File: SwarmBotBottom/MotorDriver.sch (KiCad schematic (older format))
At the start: 12 parts, among them U3 STSPIN220

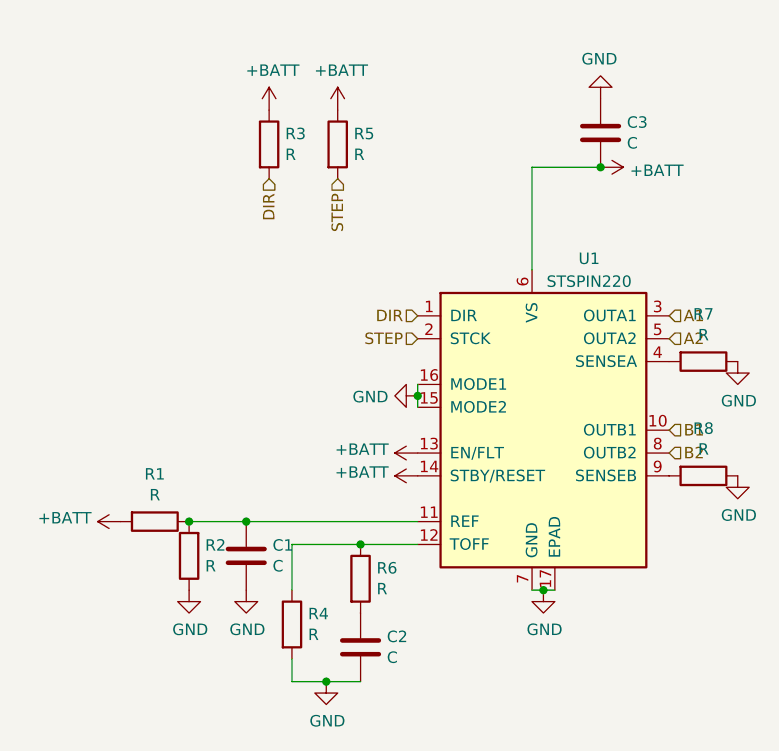
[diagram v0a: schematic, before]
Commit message: Camera routing with all sensors and motors
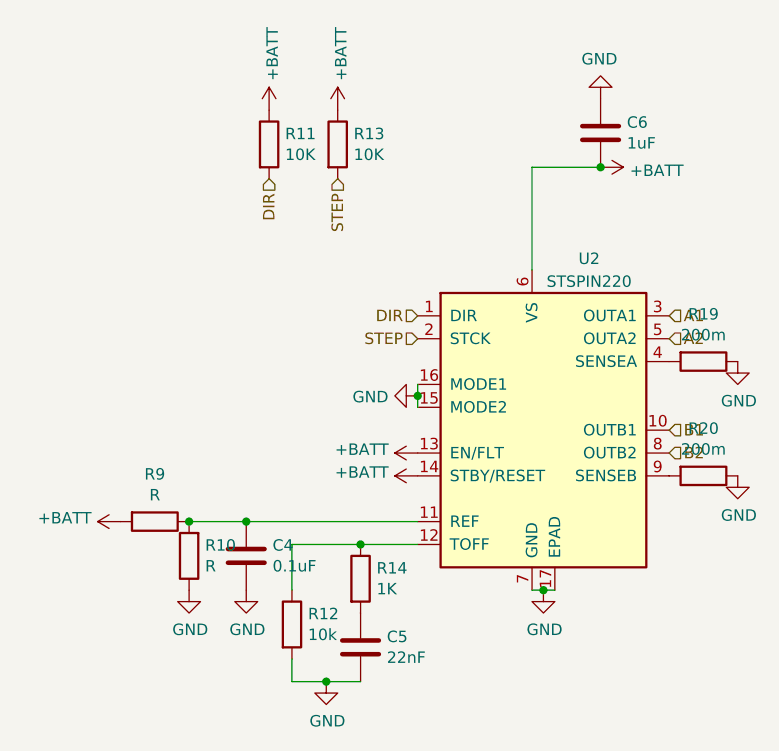
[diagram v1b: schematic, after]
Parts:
- C10: renamed from C1; value C -> 0.1uF
- C11: renamed from C2; value C -> 22nF
- C17: renamed from C3; value C -> 1uF
- R11: renamed from R3; value R -> 10K
- R12: renamed from R4; value R -> 10k
- R13: renamed from R5; value R -> 10K
- R14: renamed from R6; value R -> 1K
- R15: renamed from R7; value R -> 200m
- R16: renamed from R8; value R -> 200m
- U3: footprint Package_DFN_QFN:QFN-16-1EP_3x3mm_P0.5mm_EP1.8x1.8mm -> Package_DFN_QFN:VQFN-16-1EP_3x3mm_P0.5mm_EP1.8x1.8mm
- renumbered R1 to R8, R2 to R9

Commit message: things
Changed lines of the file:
@@
 $Descr A4 11693 8268
 encoding utf-8
-Sheet 4 4
+Sheet 3 4
 Title ""
 Date ""
@@
 AR Path="/5DAF9EF2/5DFB20FE/5DE73FE9" Ref="U1"  Part="1"
 AR Path="/5DAF9EF2/5DFB6676/5DE73FE9" Ref="U2"  Part="1"
-F 0 "U2" H 5050 3700 50  0000 C CNN
+F 0 "U1" H 5050 3700 50  0000 C CNN
 F 1 "STSPIN220" H 5050 3600 50  0000 C CNN
 F 2 "Package_DFN_QFN:VQFN-16-1EP_3x3mm_P0.5mm_EP1.8x1.8mm" H 5000 3700 50  0001 L CNN
@@
 AR Path="/5DAF9EF2/5DFB20FE/5DE7927A" Ref="R3"  Part="1"
 AR Path="/5DAF9EF2/5DFB6676/5DE7927A" Ref="R11"  Part="1"
-F 0 "R11" H 3720 1746 50  0000 L CNN
+F 0 "R3" H 3720 1746 50  0000 L CNN
 F 1 "10K" H 3720 1655 50  0000 L CNN
 F 2 "Resistor_SMD:R_0402_1005Metric" V 3580 1700 50  0001 C CNN
@@
 AR Path="/5DAF9EF2/5DFB20FE/5DE792A2" Ref="R5"  Part="1"
 AR Path="/5DAF9EF2/5DFB6676/5DE792A2" Ref="R13"  Part="1"
-F 0 "R13" H 4020 1746 50  0000 L CNN
+F 0 "R5" H 4020 1746 50  0000 L CNN
 F 1 "10K" H 4020 1655 50  0000 L CNN
 F 2 "Resistor_SMD:R_0402_1005Metric" V 3880 1700 50  0001 C CNN
@@
 AR Path="/5DAF9EF2/5DFB20FE/5DE796BD" Ref="#PWR0105"  Part="1"
 AR Path="/5DAF9EF2/5DFB6676/5DE796BD" Ref="#PWR0119"  Part="1"
-F 0 "#PWR0119" H 4300 2550 50  0001 C CNN
+F 0 "#PWR0105" H 4300 2550 50  0001 C CNN
 F 1 "GND" V 4305 2672 50  0000 R CNN
 F 2 "" H 4300 2800 50  0001 C CNN
@@
 AR Path="/5DAF9EF2/5DFB20FE/5DE79796" Ref="#PWR0106"  Part="1"
 AR Path="/5DAF9EF2/5DFB6676/5DE79796" Ref="#PWR0120"  Part="1"
-F 0 "#PWR0120" H 4300 2900 50  0001 C CNN
+F 0 "#PWR0106" H 4300 2900 50  0001 C CNN
 F 1 "+BATT" V 4315 3177 50  0000 L CNN
 F 2 "" H 4300 3050 50  0001 C CNN
@@
 AR Path="/5DAF9EF2/5DFB20FE/5DE797D2" Ref="#PWR0107"  Part="1"
 AR Path="/5DAF9EF2/5DFB6676/5DE797D2" Ref="#PWR0121"  Part="1"
-F 0 "#PWR0121" H 4300 3000 50  0001 C CNN
+F 0 "#PWR0107" H 4300 3000 50  0001 C CNN
 F 1 "+BATT" V 4315 3277 50  0000 L CNN
 F 2 "" H 4300 3150 50  0001 C CNN
@@
 AR Path="/5DAF9EF2/5DFB20FE/5DE7980C" Ref="R6"  Part="1"
 AR Path="/5DAF9EF2/5DFB6676/5DE7980C" Ref="R14"  Part="1"
-F 0 "R14" H 4120 3646 50  0000 L CNN
+F 0 "R6" H 4120 3646 50  0000 L CNN
 F 1 "1K" H 4120 3555 50  0000 L CNN
 F 2 "Resistor_SMD:R_0402_1005Metric" V 3980 3600 50  0001 C CNN
@@
 AR Path="/5DAF9EF2/5DFB20FE/5DE79862" Ref="C2"  Part="1"
 AR Path="/5DAF9EF2/5DFB6676/5DE79862" Ref="C5"  Part="1"
-F 0 "C5" H 4165 3946 50  0000 L CNN
+F 0 "C2" H 4165 3946 50  0000 L CNN
 F 1 "22nF" H 4165 3855 50  0000 L CNN
 F 2 "Capacitor_SMD:C_0402_1005Metric" H 4088 3750 50  0001 C CNN
@@
 AR Path="/5DAF9EF2/5DFB20FE/5DE798BA" Ref="R4"  Part="1"
 AR Path="/5DAF9EF2/5DFB6676/5DE798BA" Ref="R12"  Part="1"
-F 0 "R12" H 3820 3846 50  0000 L CNN
+F 0 "R4" H 3820 3846 50  0000 L CNN
 F 1 "10k" H 3820 3755 50  0000 L CNN
 F 2 "Resistor_SMD:R_0402_1005Metric" V 3680 3800 50  0001 C CNN
@@
 AR Path="/5DAF9EF2/5DFB20FE/5DE7997D" Ref="#PWR0108"  Part="1"
 AR Path="/5DAF9EF2/5DFB6676/5DE7997D" Ref="#PWR0122"  Part="1"
-F 0 "#PWR0122" H 3900 3800 50  0001 C CNN
+F 0 "#PWR0108" H 3900 3800 50  0001 C CNN
 F 1 "GND" H 3905 3877 50  0000 C CNN
 F 2 "" H 3900 4050 50  0001 C CNN
@@
 AR Path="/5DAF9EF2/5DFB20FE/5DE79A1E" Ref="C1"  Part="1"
 AR Path="/5DAF9EF2/5DFB6676/5DE79A1E" Ref="C4"  Part="1"
-F 0 "C4" H 3665 3546 50  0000 L CNN
+F 0 "C1" H 3665 3546 50  0000 L CNN
 F 1 "0.1uF" H 3665 3455 50  0000 L CNN
 F 2 "Capacitor_SMD:C_0402_1005Metric" H 3588 3350 50  0001 C CNN
@@
 AR Path="/5DAF9EF2/5DFB20FE/5DE79B51" Ref="R1"  Part="1"
 AR Path="/5DAF9EF2/5DFB6676/5DE79B51" Ref="R9"  Part="1"
-F 0 "R9" V 2943 3350 50  0000 C CNN
+F 0 "R1" V 2943 3350 50  0000 C CNN
 F 1 "R" V 3034 3350 50  0000 C CNN
 F 2 "Resistor_SMD:R_0402_1005Metric" V 3080 3350 50  0001 C CNN
@@
 AR Path="/5DAF9EF2/5DFB20FE/5DE79BA7" Ref="R2"  Part="1"
 AR Path="/5DAF9EF2/5DFB6676/5DE79BA7" Ref="R10"  Part="1"
-F 0 "R10" H 3230 3454 50  0000 R CNN
+F 0 "R2" H 3230 3454 50  0000 R CNN
 F 1 "R" H 3230 3545 50  0000 R CNN
 F 2 "Resistor_SMD:R_0402_1005Metric" V 3230 3500 50  0001 C CNN
@@
 AR Path="/5DAF9EF2/5DFB20FE/5DE79C97" Ref="#PWR0109"  Part="1"
 AR Path="/5DAF9EF2/5DFB6676/5DE79C97" Ref="#PWR0123"  Part="1"
-F 0 "#PWR0123" H 3300 3400 50  0001 C CNN
+F 0 "#PWR0109" H 3300 3400 50  0001 C CNN
 F 1 "GND" H 3305 3477 50  0000 C CNN
 F 2 "" H 3300 3650 50  0001 C CNN
@@
 AR Path="/5DAF9EF2/5DFB20FE/5DE79CBD" Ref="#PWR0110"  Part="1"
 AR Path="/5DAF9EF2/5DFB6676/5DE79CBD" Ref="#PWR0124"  Part="1"
-F 0 "#PWR0124" H 3550 3400 50  0001 C CNN
+F 0 "#PWR0110" H 3550 3400 50  0001 C CNN
 F 1 "GND" H 3555 3477 50  0000 C CNN
 F 2 "" H 3550 3650 50  0001 C CNN
@@
 AR Path="/5DAF9EF2/5DFB20FE/5DE79D20" Ref="#PWR0111"  Part="1"
 AR Path="/5DAF9EF2/5DFB6676/5DE79D20" Ref="#PWR0125"  Part="1"
-F 0 "#PWR0125" H 3000 3200 50  0001 C CNN
+F 0 "#PWR0111" H 3000 3200 50  0001 C CNN
 F 1 "+BATT" V 3015 3477 50  0000 L CNN
 F 2 "" H 3000 3350 50  0001 C CNN
@@
 AR Path="/5DAF9EF2/5DFB20FE/5DE7A1D0" Ref="#PWR0112"  Part="1"
 AR Path="/5DAF9EF2/5DFB6676/5DE7A1D0" Ref="#PWR0126"  Part="1"
-F 0 "#PWR0126" H 4850 3400 50  0001 C CNN
+F 0 "#PWR0112" H 4850 3400 50  0001 C CNN
 F 1 "GND" H 4855 3477 50  0000 C CNN
 F 2 "" H 4850 3650 50  0001 C CNN
@@
 AR Path="/5DAF9EF2/5DFB20FE/5DE7A68A" Ref="R7"  Part="1"
 AR Path="/5DAF9EF2/5DFB6676/5DE7A68A" Ref="R19"  Part="1"
-F 0 "R19" V 5343 2650 50  0000 C CNN
+F 0 "R7" V 5343 2650 50  0000 C CNN
 F 1 "200m" V 5434 2650 50  0000 C CNN
 F 2 "Resistor_SMD:R_0402_1005Metric" V 5480 2650 50  0001 C CNN
@@
 AR Path="/5DAF9EF2/5DFB20FE/5DE7A717" Ref="#PWR0113"  Part="1"
 AR Path="/5DAF9EF2/5DFB6676/5DE7A717" Ref="#PWR0127"  Part="1"
-F 0 "#PWR0127" H 5700 2400 50  0001 C CNN
+F 0 "#PWR0113" H 5700 2400 50  0001 C CNN
 F 1 "GND" H 5705 2477 50  0000 C CNN
 F 2 "" H 5700 2650 50  0001 C CNN
@@
 AR Path="/5DAF9EF2/5DFB20FE/5DE7A78F" Ref="R8"  Part="1"
 AR Path="/5DAF9EF2/5DFB6676/5DE7A78F" Ref="R20"  Part="1"
-F 0 "R20" V 5343 3150 50  0000 C CNN
+F 0 "R8" V 5343 3150 50  0000 C CNN
 F 1 "200m" V 5434 3150 50  0000 C CNN
 F 2 "Resistor_SMD:R_0402_1005Metric" V 5480 3150 50  0001 C CNN
@@
 AR Path="/5DAF9EF2/5DFB20FE/5DE7A796" Ref="#PWR0114"  Part="1"
 AR Path="/5DAF9EF2/5DFB6676/5DE7A796" Ref="#PWR0128"  Part="1"
-F 0 "#PWR0128" H 5700 2900 50  0001 C CNN
+F 0 "#PWR0114" H 5700 2900 50  0001 C CNN
 F 1 "GND" H 5705 2977 50  0000 C CNN
 F 2 "" H 5700 3150 50  0001 C CNN
@@
 AR Path="/5DAF9EF2/5DFB20FE/5DE80E70" Ref="C3"  Part="1"
 AR Path="/5DAF9EF2/5DFB6676/5DE80E70" Ref="C6"  Part="1"
-F 0 "C6" H 5215 1696 50  0000 L CNN
+F 0 "C3" H 5215 1696 50  0000 L CNN
 F 1 "1uF" H 5215 1605 50  0000 L CNN
 F 2 "Capacitor_SMD:C_0402_1005Metric" H 5138 1500 50  0001 C CNN
@@
 AR Path="/5DAF9EF2/5DFB20FE/5DE80F5C" Ref="#PWR0115"  Part="1"
 AR Path="/5DAF9EF2/5DFB6676/5DE80F5C" Ref="#PWR0129"  Part="1"
-F 0 "#PWR0129" H 5100 1650 50  0001 C CNN
+F 0 "#PWR0115" H 5100 1650 50  0001 C CNN
 F 1 "+BATT" V 5115 1928 50  0000 L CNN
 F 2 "" H 5100 1800 50  0001 C CNN
@@
 AR Path="/5DAF9EF2/5DFB20FE/5DE80FD8" Ref="#PWR0116"  Part="1"
 AR Path="/5DAF9EF2/5DFB6676/5DE80FD8" Ref="#PWR0130"  Part="1"
-F 0 "#PWR0130" H 5100 1250 50  0001 C CNN
+F 0 "#PWR0116" H 5100 1250 50  0001 C CNN
 F 1 "GND" H 5105 1327 50  0000 C CNN
 F 2 "" H 5100 1500 50  0001 C CNN
@@
 AR Path="/5DAF9EF2/5DFB20FE/5DEA39A3" Ref="#PWR0117"  Part="1"
 AR Path="/5DAF9EF2/5DFB6676/5DEA39A3" Ref="#PWR0131"  Part="1"
-F 0 "#PWR0131" H 3650 1400 50  0001 C CNN
+F 0 "#PWR0117" H 3650 1400 50  0001 C CNN
 F 1 "+BATT" V 3665 1678 50  0000 L CNN
 F 2 "" H 3650 1550 50  0001 C CNN
@@
 AR Path="/5DAF9EF2/5DFB20FE/5DEA3D6C" Ref="#PWR0118"  Part="1"
 AR Path="/5DAF9EF2/5DFB6676/5DEA3D6C" Ref="#PWR0132"  Part="1"
-F 0 "#PWR0132" H 3950 1400 50  0001 C CNN
+F 0 "#PWR0118" H 3950 1400 50  0001 C CNN
 F 1 "+BATT" V 3965 1678 50  0000 L CNN
 F 2 "" H 3950 1550 50  0001 C CNN

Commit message: Final Design
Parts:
- removed R9: R, Resistor_SMD:R_0402_1005Metric, symbol Device:R
- R8: value R -> 1K
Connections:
- net +BATT: no longer R8.2, U3.13 (EN/FLT)
- new net CURRSET: R8.2
- new net STEPPEREN: U3.13 (EN/FLT)
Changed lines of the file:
@@
 AR Path="/5DAF9EF2/5DFB20FE/5DE796BD" Ref="#PWR0105"  Part="1"
 AR Path="/5DAF9EF2/5DFB6676/5DE796BD" Ref="#PWR0119"  Part="1"
-F 0 "#PWR0105" H 4300 2550 50  0001 C CNN
+F 0 "#PWR0119" H 4300 2550 50  0001 C CNN
 F 1 "GND" V 4305 2672 50  0000 R CNN
 F 2 "" H 4300 2800 50  0001 C CNN
@@
 Wire Wire Line
 	4300 2800 4300 2850
-$Comp
-L power:+BATT #PWR0127
-U 1 1 5DE79796
-P 4300 3050
-AR Path="/5DAF9EF2/5DEAE9FD/5DE79796" Ref="#PWR0127"  Part="1"
-AR Path="/5DAF9EF2/5DEAF8AB/5DE79796" Ref="#PWR0110"  Part="1"
-AR Path="/5DAF9EF2/5DFB20FE/5DE79796" Ref="#PWR0106"  Part="1"
-AR Path="/5DAF9EF2/5DFB6676/5DE79796" Ref="#PWR0120"  Part="1"
-F 0 "#PWR0106" H 4300 2900 50  0001 C CNN
-F 1 "+BATT" V 4315 3177 50  0000 L CNN
-F 2 "" H 4300 3050 50  0001 C CNN
-F 3 "" H 4300 3050 50  0001 C CNN
-	1    4300 3050
-	0    -1   -1   0
-$EndComp
 $Comp
 L power:+BATT #PWR0128
@@
 AR Path="/5DAF9EF2/5DFB20FE/5DE797D2" Ref="#PWR0107"  Part="1"
 AR Path="/5DAF9EF2/5DFB6676/5DE797D2" Ref="#PWR0121"  Part="1"
-F 0 "#PWR0107" H 4300 3000 50  0001 C CNN
+F 0 "#PWR0121" H 4300 3000 50  0001 C CNN
 F 1 "+BATT" V 4315 3277 50  0000 L CNN
 F 2 "" H 4300 3150 50  0001 C CNN
@@
 AR Path="/5DAF9EF2/5DFB20FE/5DE7997D" Ref="#PWR0108"  Part="1"
 AR Path="/5DAF9EF2/5DFB6676/5DE7997D" Ref="#PWR0122"  Part="1"
-F 0 "#PWR0108" H 3900 3800 50  0001 C CNN
+F 0 "#PWR0122" H 3900 3800 50  0001 C CNN
 F 1 "GND" H 3905 3877 50  0000 C CNN
 F 2 "" H 3900 4050 50  0001 C CNN
@@
 AR Path="/5DAF9EF2/5DFB6676/5DE79B51" Ref="R9"  Part="1"
 F 0 "R1" V 2943 3350 50  0000 C CNN
-F 1 "R" V 3034 3350 50  0000 C CNN
+F 1 "1K" V 3034 3350 50  0000 C CNN
 F 2 "Resistor_SMD:R_0402_1005Metric" V 3080 3350 50  0001 C CNN
 F 3 "~" H 3150 3350 50  0001 C CNN
@@
 	0    1    1    0
 $EndComp
-$Comp
-L Device:R R9
-U 1 1 5DE79BA7
-P 3300 3500
-AR Path="/5DAF9EF2/5DEAE9FD/5DE79BA7" Ref="R9"  Part="1"
-AR Path="/5DAF9EF2/5DEAF8AB/5DE79BA7" Ref="R9"  Part="1"
-AR Path="/5DAF9EF2/5DFB20FE/5DE79BA7" Ref="R2"  Part="1"
-AR Path="/5DAF9EF2/5DFB6676/5DE79BA7" Ref="R10"  Part="1"
-F 0 "R2" H 3230 3454 50  0000 R CNN
-F 1 "R" H 3230 3545 50  0000 R CNN
-F 2 "Resistor_SMD:R_0402_1005Metric" V 3230 3500 50  0001 C CNN
-F 3 "~" H 3300 3500 50  0001 C CNN
-	1    3300 3500
-	-1   0    0    1
-$EndComp
 Wire Wire Line
 	3300 3350 3550 3350
-Connection ~ 3300 3350
 Connection ~ 3550 3350
-$Comp
-L power:GND #PWR0130
-U 1 1 5DE79C97
-P 3300 3650
-AR Path="/5DAF9EF2/5DEAE9FD/5DE79C97" Ref="#PWR0130"  Part="1"
-AR Path="/5DAF9EF2/5DEAF8AB/5DE79C97" Ref="#PWR0113"  Part="1"
-AR Path="/5DAF9EF2/5DFB20FE/5DE79C97" Ref="#PWR0109"  Part="1"
-AR Path="/5DAF9EF2/5DFB6676/5DE79C97" Ref="#PWR0123"  Part="1"
-F 0 "#PWR0109" H 3300 3400 50  0001 C CNN
-F 1 "GND" H 3305 3477 50  0000 C CNN
-F 2 "" H 3300 3650 50  0001 C CNN
-F 3 "" H 3300 3650 50  0001 C CNN
-	1    3300 3650
-	1    0    0    -1
-$EndComp
 $Comp
 L power:GND #PWR0131
@@
 AR Path="/5DAF9EF2/5DFB20FE/5DE79CBD" Ref="#PWR0110"  Part="1"
 AR Path="/5DAF9EF2/5DFB6676/5DE79CBD" Ref="#PWR0124"  Part="1"
-F 0 "#PWR0110" H 3550 3400 50  0001 C CNN
+F 0 "#PWR0124" H 3550 3400 50  0001 C CNN
 F 1 "GND" H 3555 3477 50  0000 C CNN
 F 2 "" H 3550 3650 50  0001 C CNN
@@
 	1    3550 3650
 	1    0    0    -1
-$EndComp
-$Comp
-L power:+BATT #PWR0132
-U 1 1 5DE79D20
-P 3000 3350
-AR Path="/5DAF9EF2/5DEAE9FD/5DE79D20" Ref="#PWR0132"  Part="1"
-AR Path="/5DAF9EF2/5DEAF8AB/5DE79D20" Ref="#PWR0116"  Part="1"
-AR Path="/5DAF9EF2/5DFB20FE/5DE79D20" Ref="#PWR0111"  Part="1"
-AR Path="/5DAF9EF2/5DFB6676/5DE79D20" Ref="#PWR0125"  Part="1"
-F 0 "#PWR0111" H 3000 3200 50  0001 C CNN
-F 1 "+BATT" V 3015 3477 50  0000 L CNN
-F 2 "" H 3000 3350 50  0001 C CNN
-F 3 "" H 3000 3350 50  0001 C CNN
-	1    3000 3350
-	0    -1   -1   0
 $EndComp
 Wire Wire Line
@@
 AR Path="/5DAF9EF2/5DFB20FE/5DE7A1D0" Ref="#PWR0112"  Part="1"
 AR Path="/5DAF9EF2/5DFB6676/5DE7A1D0" Ref="#PWR0126"  Part="1"
-F 0 "#PWR0112" H 4850 3400 50  0001 C CNN
+F 0 "#PWR0126" H 4850 3400 50  0001 C CNN
 F 1 "GND" H 4855 3477 50  0000 C CNN
 F 2 "" H 4850 3650 50  0001 C CNN
@@
 AR Path="/5DAF9EF2/5DFB20FE/5DE7A717" Ref="#PWR0113"  Part="1"
 AR Path="/5DAF9EF2/5DFB6676/5DE7A717" Ref="#PWR0127"  Part="1"
-F 0 "#PWR0113" H 5700 2400 50  0001 C CNN
+F 0 "#PWR0127" H 5700 2400 50  0001 C CNN
 F 1 "GND" H 5705 2477 50  0000 C CNN
 F 2 "" H 5700 2650 50  0001 C CNN
@@
 AR Path="/5DAF9EF2/5DFB20FE/5DE7A796" Ref="#PWR0114"  Part="1"
 AR Path="/5DAF9EF2/5DFB6676/5DE7A796" Ref="#PWR0128"  Part="1"
-F 0 "#PWR0114" H 5700 2900 50  0001 C CNN
+F 0 "#PWR0128" H 5700 2900 50  0001 C CNN
 F 1 "GND" H 5705 2977 50  0000 C CNN
 F 2 "" H 5700 3150 50  0001 C CNN
@@
 AR Path="/5DAF9EF2/5DFB20FE/5DE80F5C" Ref="#PWR0115"  Part="1"
 AR Path="/5DAF9EF2/5DFB6676/5DE80F5C" Ref="#PWR0129"  Part="1"
-F 0 "#PWR0115" H 5100 1650 50  0001 C CNN
+F 0 "#PWR0129" H 5100 1650 50  0001 C CNN
 F 1 "+BATT" V 5115 1928 50  0000 L CNN
 F 2 "" H 5100 1800 50  0001 C CNN
@@
 AR Path="/5DAF9EF2/5DFB20FE/5DE80FD8" Ref="#PWR0116"  Part="1"
 AR Path="/5DAF9EF2/5DFB6676/5DE80FD8" Ref="#PWR0130"  Part="1"
-F 0 "#PWR0116" H 5100 1250 50  0001 C CNN
+F 0 "#PWR0130" H 5100 1250 50  0001 C CNN
 F 1 "GND" H 5105 1327 50  0000 C CNN
 F 2 "" H 5100 1500 50  0001 C CNN
@@
 AR Path="/5DAF9EF2/5DFB20FE/5DEA39A3" Ref="#PWR0117"  Part="1"
 AR Path="/5DAF9EF2/5DFB6676/5DEA39A3" Ref="#PWR0131"  Part="1"
-F 0 "#PWR0117" H 3650 1400 50  0001 C CNN
+F 0 "#PWR0131" H 3650 1400 50  0001 C CNN
 F 1 "+BATT" V 3665 1678 50  0000 L CNN
 F 2 "" H 3650 1550 50  0001 C CNN
@@
 AR Path="/5DAF9EF2/5DFB20FE/5DEA3D6C" Ref="#PWR0118"  Part="1"
 AR Path="/5DAF9EF2/5DFB6676/5DEA3D6C" Ref="#PWR0132"  Part="1"
-F 0 "#PWR0118" H 3950 1400 50  0001 C CNN
+F 0 "#PWR0132" H 3950 1400 50  0001 C CNN
 F 1 "+BATT" V 3965 1678 50  0000 L CNN
 F 2 "" H 3950 1550 50  0001 C CNN
@@
 	1    0    0    -1
 $EndComp
+Text HLabel 3000 3350 0    50   Input ~ 0
+CURRSET
+Text HLabel 4300 3050 0    50   Input ~ 0
+STEPPEREN
 $EndSCHEMATC
